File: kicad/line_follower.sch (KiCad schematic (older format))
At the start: 48 parts, among them J1 XT30PW-M, M1 MOTOR_ENC, M2 MOTOR_ENC, Q1 ALS-PT19-315C_L177_TR8, Q2 ALS-PT19-315C_L177_TR8, Q3 ALS-PT19-315C_L177_TR8, Q4 ALS-PT19-315C_L177_TR8, Q5 ALS-PT19-315C_L177_TR8, SW1 SW_Push, U1 A4950E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

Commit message: schematic: Removed comment
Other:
- note removed: "Has pull up on reset!"
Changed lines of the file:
@@
 Text Notes 1150 4300 0    50   ~ 0
 GPIO5 has a pull-up on X1
-Text Notes 3400 1950 0    50   ~ 0
-Has pull up on reset!
 Text Label 650  1350 0    70   ~ 0
 LINE_SENSOR0

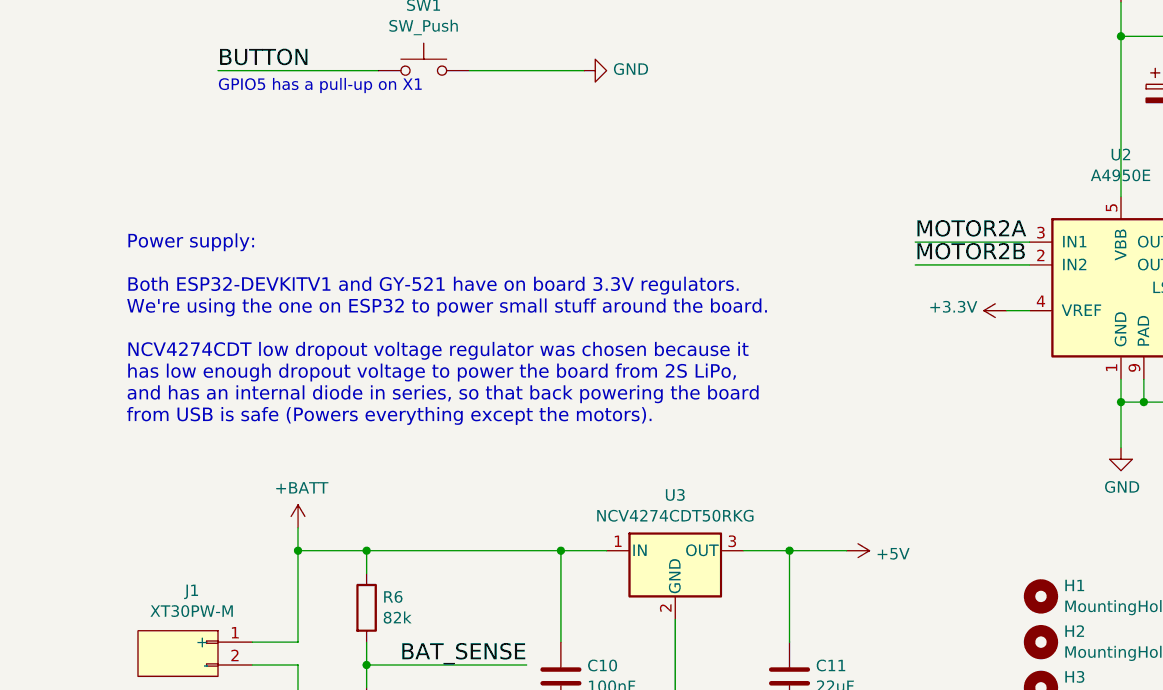
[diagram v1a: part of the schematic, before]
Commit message: schematic: Modified power supply LDO because of availability at Mouser.
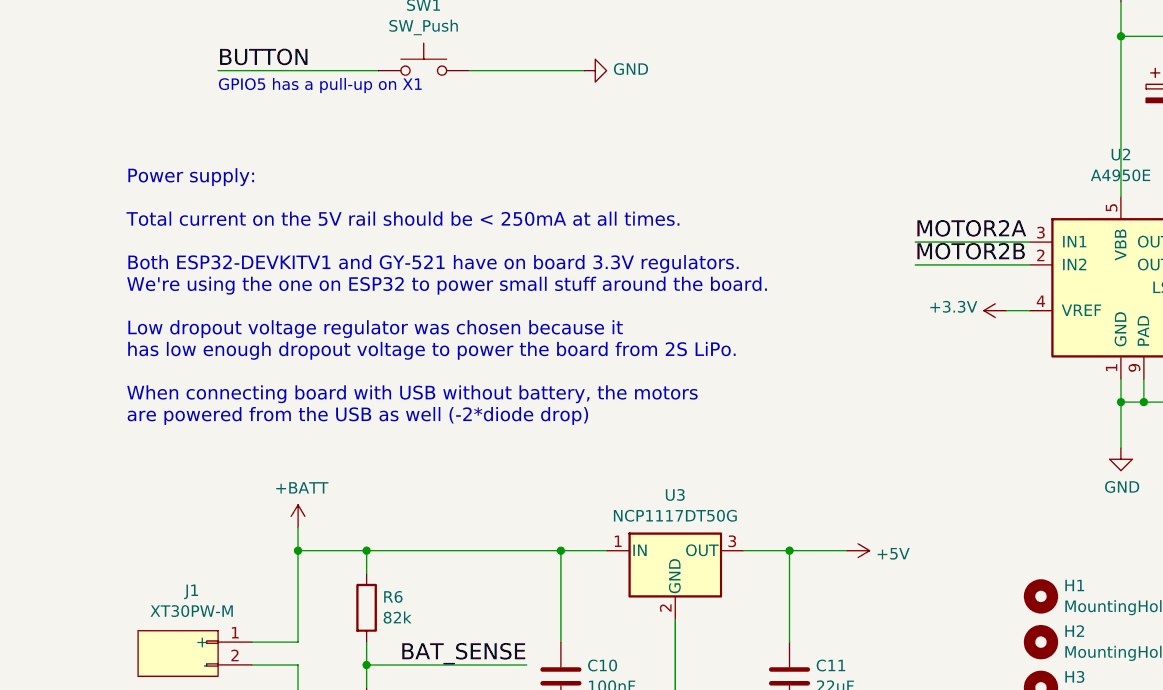
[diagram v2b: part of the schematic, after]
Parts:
- U3: value NCV4274CDT50RKG -> NCP1117DT50G
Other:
- note added: "Power supply:\n\nTotal current on the 5V rail should be < 250mA at all times.\n\nBoth ESP32-DEVKITV1 and GY-521 have on board 3.3V regulators.\nWe're using the one on ESP32 to power small stuff around the board.\n\nLow dropout voltage regulator was chosen because it\nhas low enough dropout voltage to power the board from 2S LiPo.\n\nWhen connecting board with USB without battery, the motors\nare 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"
- note removed: "Power supply:\n\nBoth ESP32-DEVKITV1 and GY-521 have on board 3.3V regulators.\nWe're using the one on ESP32 to power small stuff around the board.\n\nNCV4274CDT low dropout voltage regulator was chosen because it\nhas low enough dropout voltage to power the board from 2S LiPo,\nand has an internal diode in series, so that back powering the board\nfrom USB is safe (Powers everything except the mo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"
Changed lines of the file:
@@
 ACCEL_INT
 Text Notes 750  5750 0    59   ~ 0
-Power supply:\n\nBoth ESP32-DEVKITV1 and GY-521 have on board 3.3V regulators.\nWe're using the one on ESP32 to power small stuff around the board.\n\nNCV4274CDT low dropout voltage regulator was chosen because it\nhas low enough dropout voltage to power the board from 2S LiPo,\nand has an internal diode in series, so that back powering the board\nfrom USB is safe (Powers everything except the motors).
+Power supply:\n\nTotal current on the 5V rail should be < 250mA at all times.\n\nBoth ESP32-DEVKITV1 and GY-521 have on board 3.3V regulators.\nWe're using the one on ESP32 to power small stuff around the board.\n\nLow dropout voltage regulator was chosen because it\nhas low enough dropout voltage to power the board from 2S LiPo.\n\nWhen connecting board with USB without battery, the motors\nare powered from the USB as well (-2*diode drop)
 Text Notes 2600 1050 0    59   ~ 0
 UART TX/RX\nconnected to USB
@@
 P 3150 6300
 F 0 "U3" H 3150 6542 50  0000 C CNN
-F 1 "NCV4274CDT50RKG" H 3150 6451 50  0000 C CNN
+F 1 "NCP1117DT50G" H 3150 6451 50  0000 C CNN
 F 2 "Package_TO_SOT_SMD:TO-252-2" H 3175 6150 50  0001 L CIN
 F 3 "http://www.st.com/content/ccc/resource/technical/document/datasheet/41/4f/b3/b0/12/d4/47/88/CD00000444.pdf/files/CD00000444.pdf/jcr:content/translations/en.CD00000444.pdf" H 3150 6250 50  0001 C CNN

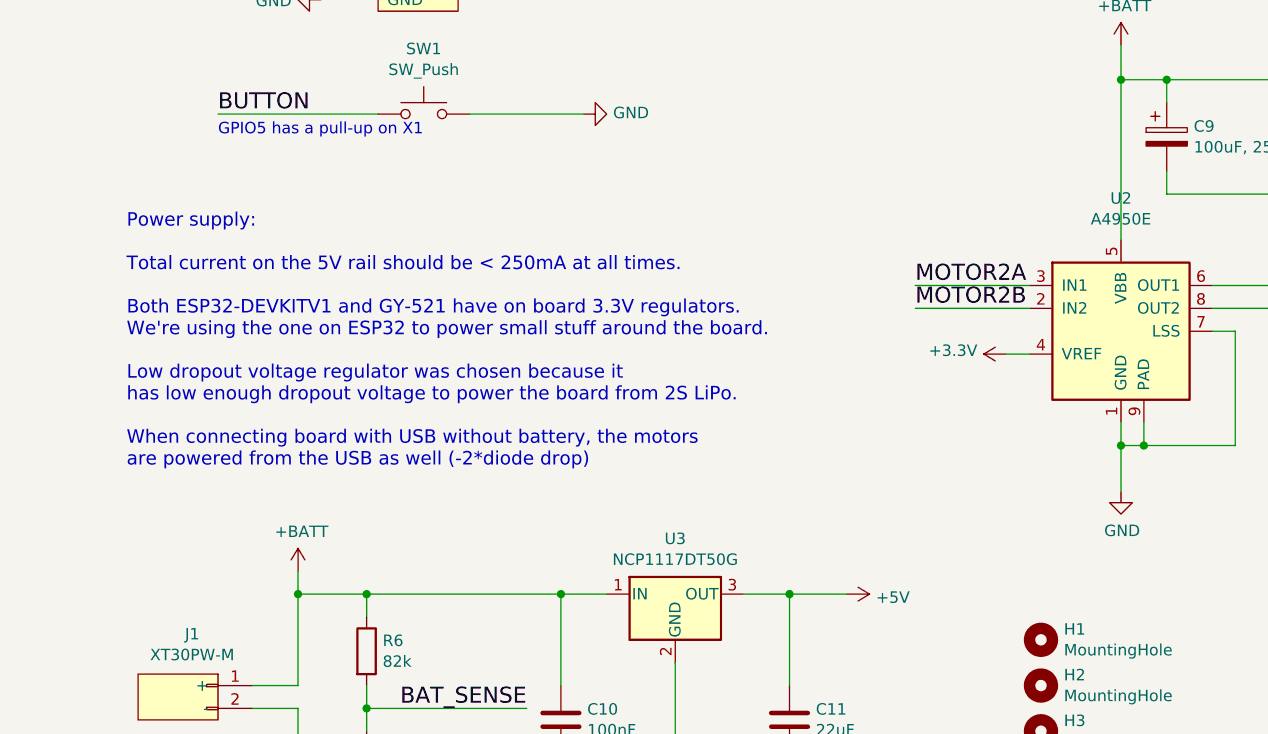
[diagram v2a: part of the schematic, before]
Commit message: schematic: Changed the 5V regulator again
the previous one had wrong pinout
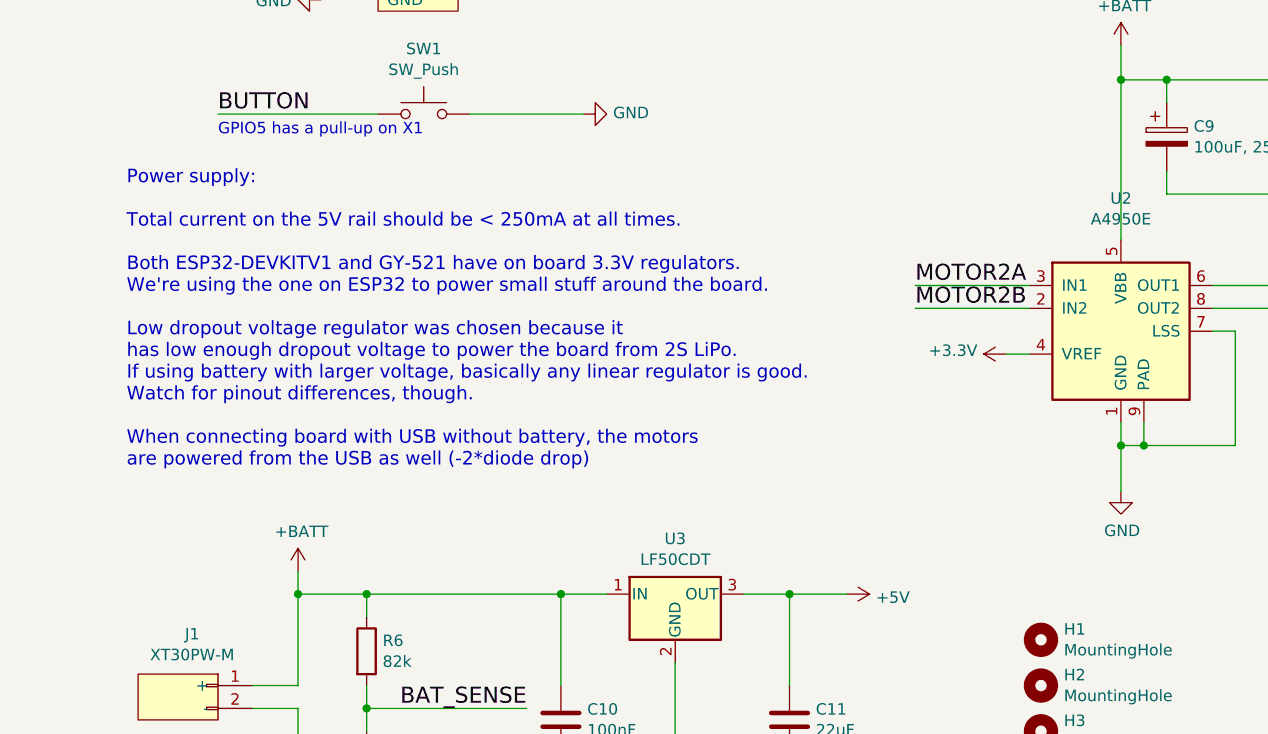
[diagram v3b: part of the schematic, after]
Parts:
- U3: value NCP1117DT50G -> LF50CDT
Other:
- note added: "Power supply:\n\nTotal current on the 5V rail should be < 250mA at all times.\n\nBoth ESP32-DEVKITV1 and GY-521 have on board 3.3V regulators.\nWe're using the one on ESP32 to power small stuff around the board.\n\nLow dropout voltage regulator was chosen because it\nhas low enough dropout voltage to power the board from 2S LiPo.\nIf using battery with larger voltage, basically any linear regulat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"
- note removed: "Power supply:\n\nTotal current on the 5V rail should be < 250mA at all times.\n\nBoth ESP32-DEVKITV1 and GY-521 have on board 3.3V regulators.\nWe're using the one on ESP32 to power small stuff around the board.\n\nLow dropout voltage regulator was chosen because it\nhas low enough dropout voltage to power the board from 2S LiPo.\n\nWhen connecting board with USB without battery, the motors\nare 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"
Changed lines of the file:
@@
 ACCEL_INT
 Text Notes 750  5750 0    59   ~ 0
-Power supply:\n\nTotal current on the 5V rail should be < 250mA at all times.\n\nBoth ESP32-DEVKITV1 and GY-521 have on board 3.3V regulators.\nWe're using the one on ESP32 to power small stuff around the board.\n\nLow dropout voltage regulator was chosen because it\nhas low enough dropout voltage to power the board from 2S LiPo.\n\nWhen connecting board with USB without battery, the motors\nare powered from the USB as well (-2*diode drop)
+Power supply:\n\nTotal current on the 5V rail should be < 250mA at all times.\n\nBoth ESP32-DEVKITV1 and GY-521 have on board 3.3V regulators.\nWe're using the one on ESP32 to power small stuff around the board.\n\nLow dropout voltage regulator was chosen because it\nhas low enough dropout voltage to power the board from 2S LiPo.\nIf using battery with larger voltage, basically any linear regulator is good.\nWatch for pinout differences, though.\n\nWhen connecting board with USB without battery, the motors\nare powered from the USB as well (-2*diode drop)
 Text Notes 2600 1050 0    59   ~ 0
 UART TX/RX\nconnected to USB
@@
 P 3150 6300
 F 0 "U3" H 3150 6542 50  0000 C CNN
-F 1 "NCP1117DT50G" H 3150 6451 50  0000 C CNN
+F 1 "LF50CDT" H 3150 6451 50  0000 C CNN
 F 2 "Package_TO_SOT_SMD:TO-252-2" H 3175 6150 50  0001 L CIN
 F 3 "http://www.st.com/content/ccc/resource/technical/document/datasheet/41/4f/b3/b0/12/d4/47/88/CD00000444.pdf/files/CD00000444.pdf/jcr:content/translations/en.CD00000444.pdf" H 3150 6250 50  0001 C CNN
